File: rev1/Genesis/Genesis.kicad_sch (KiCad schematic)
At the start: 0 parts

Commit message: More updates.
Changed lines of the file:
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@@
 	(sheet
 		(at 100.33 90.17)
-		(size 19.05 21.59)
+		(size 19.05 24.13)
 		(exclude_from_sim no)
 		(in_bom yes)
@@
 		)
 		(property "Sheetfile" "../../kicad-import/adafruit-ethernet/Adafruit Ethernet FeatherWing.kicad_sch"
-			(at 100.33 112.3446 0)
+			(at 100.33 114.8846 0)
 			(effects
 				(font

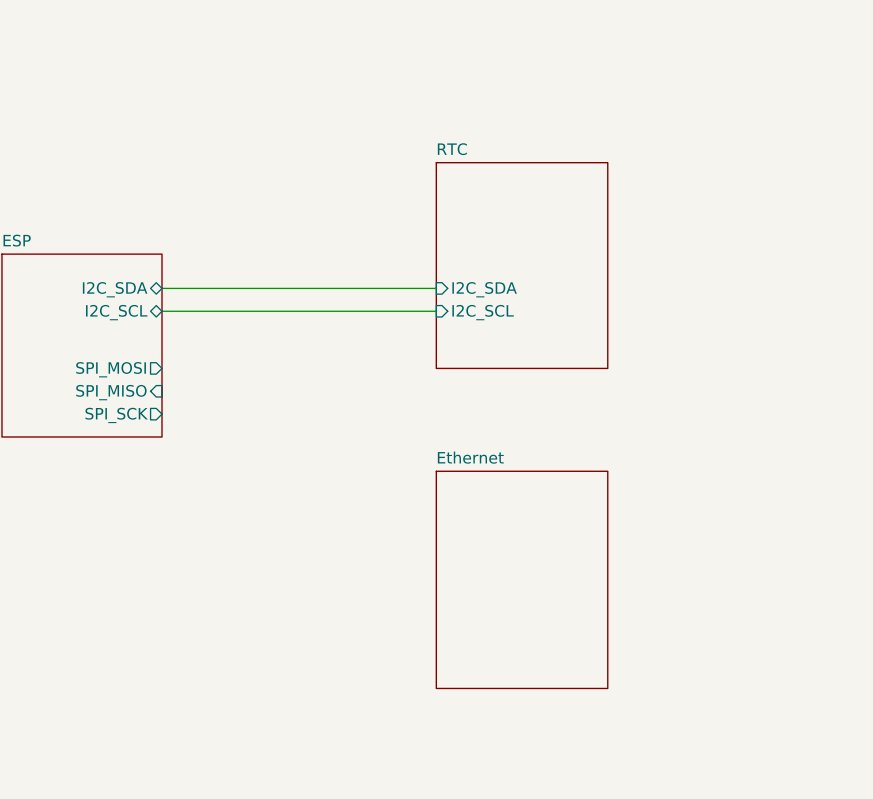
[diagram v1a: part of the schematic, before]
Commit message: Add and connect SPI sheet labels to Ethernet page.
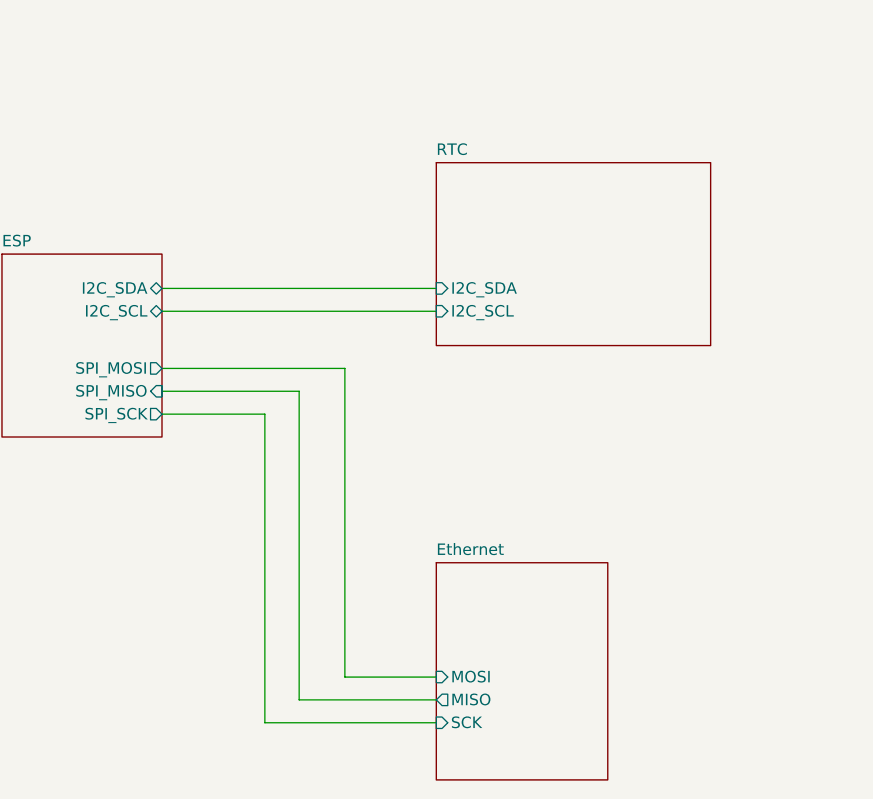
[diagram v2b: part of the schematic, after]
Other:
- sheet Ethernet ports: added MISO, MOSI, SCK; removed none
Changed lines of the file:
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@@
+	(wire
+		(pts
+			(xy 85.09 81.28) (xy 85.09 115.57)
+		)
+		(stroke
+			(width 0)
+			(type default)
+		)
+	)
+	(wire
+		(pts
+			(xy 85.09 115.57) (xy 100.33 115.57)
+		)
+		(stroke
+			(width 0)
+			(type default)
+		)
+	)
 	(wire
 		(pts
@@
 	(wire
 		(pts
+			(xy 69.85 78.74) (xy 90.17 78.74)
+		)
+		(stroke
+			(width 0)
+			(type default)
+		)
+	)
+	(wire
+		(pts
 			(xy 69.85 72.39) (xy 100.33 72.39)
+		)
+		(stroke
+			(width 0)
+			(type default)
+		)
+	)
+	(wire
+		(pts
+			(xy 81.28 118.11) (xy 100.33 118.11)
+		)
+		(stroke
+			(width 0)
+			(type default)
+		)
+	)
+	(wire
+		(pts
+			(xy 90.17 78.74) (xy 90.17 113.03)
+		)
+		(stroke
+			(width 0)
+			(type default)
+		)
+	)
+	(wire
+		(pts
+			(xy 69.85 81.28) (xy 85.09 81.28)
+		)
+		(stroke
+			(width 0)
+			(type default)
+		)
+	)
+	(wire
+		(pts
+			(xy 81.28 83.82) (xy 81.28 118.11)
+		)
+		(stroke
+			(width 0)
+			(type default)
+		)
+	)
+	(wire
+		(pts
+			(xy 90.17 113.03) (xy 100.33 113.03)
+		)
+		(stroke
+			(width 0)
+			(type default)
+		)
+	)
+	(wire
+		(pts
+			(xy 69.85 83.82) (xy 81.28 83.82)
 		)
 		(stroke
@@
 	)
 	(sheet
-		(at 100.33 90.17)
+		(at 100.33 100.33)
 		(size 19.05 24.13)
 		(exclude_from_sim no)
@@
 		)
 		(property "Sheetname" "Ethernet"
-			(at 100.33 89.4584 0)
+			(at 100.33 99.6184 0)
 			(effects
 				(font
@@
 		)
 		(property "Sheetfile" "../../kicad-import/adafruit-ethernet/Adafruit Ethernet FeatherWing.kicad_sch"
-			(at 100.33 114.8846 0)
+			(at 100.33 125.0446 0)
 			(effects
 				(font
@@
 				(justify left top)
 				(hide yes)
+			)
+		)
+		(pin "MISO" output
+			(at 100.33 115.57 180)
+			(effects
+				(font
+					(size 1.27 1.27)
+				)
+				(justify left)
+			)
+		)
+		(pin "MOSI" input
+			(at 100.33 113.03 180)
+			(effects
+				(font
+					(size 1.27 1.27)
+				)
+				(justify left)
+			)
+		)
+		(pin "SCK" input
+			(at 100.33 118.11 180)
+			(effects
+				(font
+					(size 1.27 1.27)
+				)
+				(justify left)
 			)
 		)
@@
 	(sheet
 		(at 100.33 55.88)
-		(size 19.05 22.86)
+		(size 30.48 20.32)
 		(exclude_from_sim no)
 		(in_bom yes)
@@
 		)
 		(property "Sheetfile" "../../kicad-import/adafruit-datalogger/adalogger featherwing.kicad_sch"
-			(at 100.33 79.3246 0)
-			(effects
-				(font
+			(at 100.33 76.7846 0)
+			(effects
+				(font

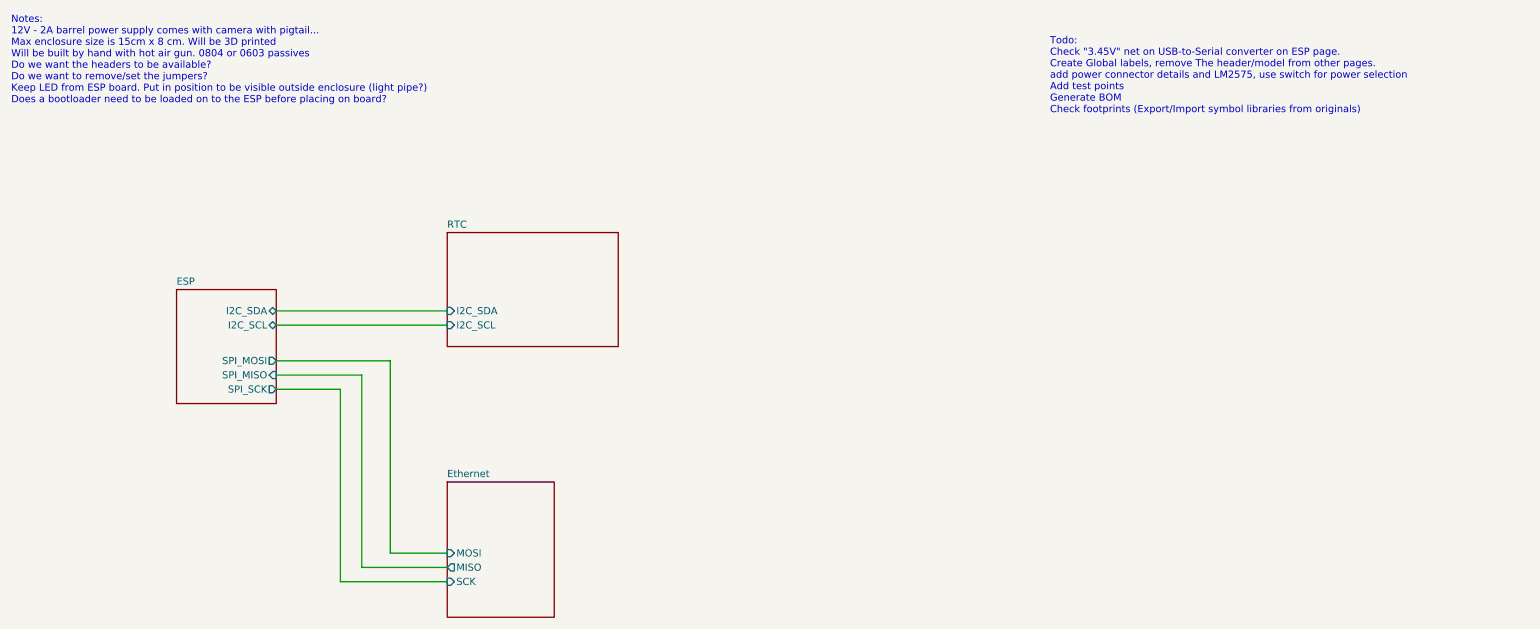
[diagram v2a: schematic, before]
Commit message: Improve sheet labels. Remove extra model and headers from ETH and RTC pages.
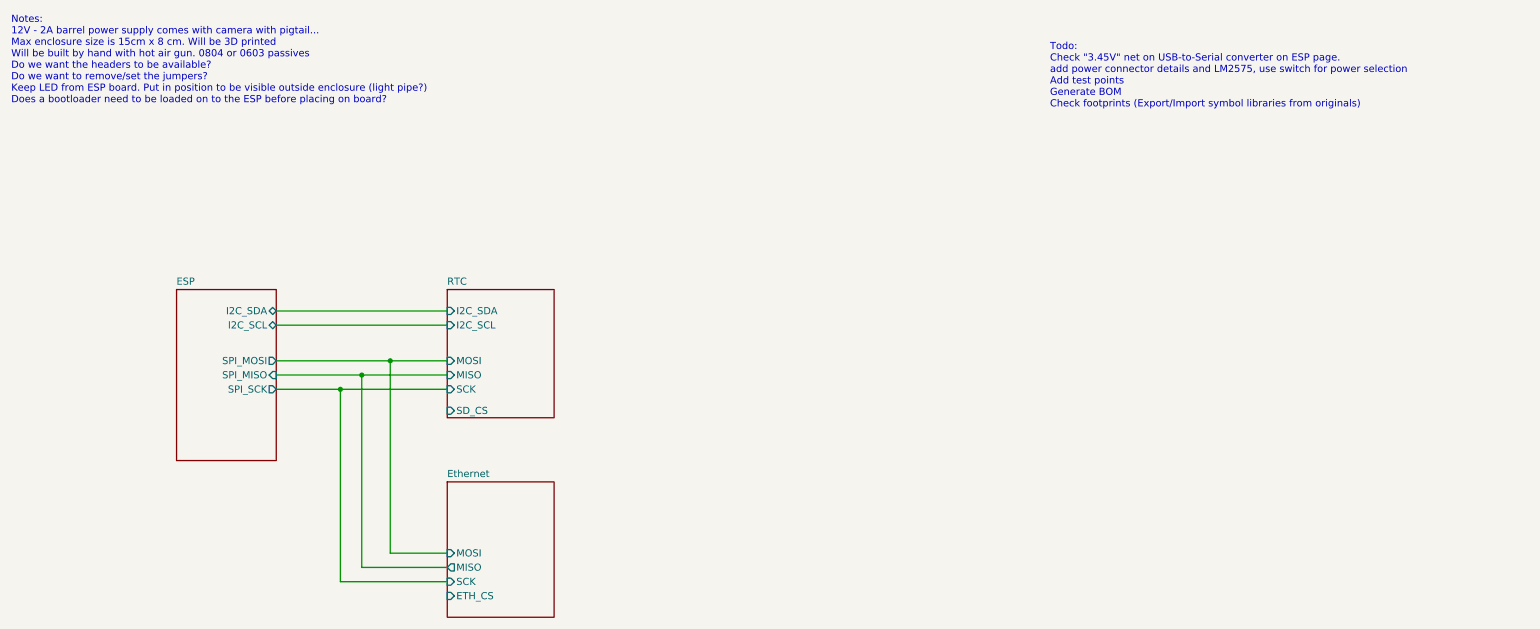
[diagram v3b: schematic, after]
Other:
- sheet Ethernet ports: added ETH_CS; removed none
- sheet RTC ports: added MISO, MOSI, SCK, SD_CS; removed none
- note added: "Todo: Check "3.45V" net on USB-to-Serial converter on ESP page. add power connector details and LM2575, use switch for power selection Add test points Generate BOM Check footprints (Export/Import symbol libraries from originals)"
- note removed: "Todo: Check "3.45V" net on USB-to-Serial converter on ESP page. Create Global labels, remove The header/model from other pages. add power connector details and LM2575, use switch for power selection Add test points Generate BOM Check footprints (Export/Import symbol libraries from originals)"
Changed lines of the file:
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@@
 		)
 	)
-	(text "Todo:\nCheck \"3.45V\" net on USB-to-Serial converter on ESP page.\nCreate Global labels, remove The header/model from other pages.\nadd power connector details and LM2575, use switch for power selection\nAdd test points\nGenerate BOM\nCheck footprints (Export/Import symbol libraries from originals)"
+	(text "Todo:\nCheck \"3.45V\" net on USB-to-Serial converter on ESP page.\nadd power connector details and LM2575, use switch for power selection\nAdd test points\nGenerate BOM\nCheck footprints (Export/Import symbol libraries from originals)"
 		(exclude_from_sim no)
 		(at 207.772 27.94 0)
@@
 		)
 	)
+	(junction
+		(at 85.09 81.28)
+		(diameter 0)
+		(color 0 0 0 0)
+	)
+	(junction
+		(at 81.28 83.82)
+		(diameter 0)
+		(color 0 0 0 0)
+	)
+	(junction
+		(at 90.17 78.74)
+		(diameter 0)
+		(color 0 0 0 0)
+	)
 	(wire
 		(pts
@@
 	(wire
 		(pts
+			(xy 81.28 83.82) (xy 100.33 83.82)
+		)
+		(stroke
+			(width 0)
+			(type default)
+		)
+	)
+	(wire
+		(pts
 			(xy 90.17 113.03) (xy 100.33 113.03)
 		)
@@
 		(pts
 			(xy 69.85 83.82) (xy 81.28 83.82)
+		)
+		(stroke
+			(width 0)
+			(type default)
+		)
+	)
+	(wire
+		(pts
+			(xy 85.09 81.28) (xy 100.33 81.28)
+		)
+		(stroke
+			(width 0)
+			(type default)
+		)
+	)
+	(wire
+		(pts
+			(xy 90.17 78.74) (xy 100.33 78.74)
 		)
 		(stroke
@@
 	(sheet
 		(at 52.07 66.04)
-		(size 17.78 20.32)
+		(size 17.78 30.48)
 		(exclude_from_sim no)
 		(in_bom yes)
@@
 		)
 		(property "Sheetfile" "../../kicad-import/adafruit-feather/Adafruit ESP32 Feather V2.kicad_sch"
-			(at 52.07 86.9446 0)
+			(at 52.07 97.1046 0)
 			(effects
 				(font
@@
 			)
 		)
+		(pin "ETH_CS" input
+			(at 100.33 120.65 180)
+			(effects
+				(font
+					(size 1.27 1.27)
+				)
+				(justify left)
+			)
+		)
 		(instances
 			(project "Genesis"
@@
 	)
 	(sheet
-		(at 100.33 55.88)
-		(size 30.48 20.32)
+		(at 100.33 66.04)
+		(size 19.05 22.86)
 		(exclude_from_sim no)
 		(in_bom yes)
@@
 		)
 		(property "Sheetname" "RTC"
-			(at 100.33 55.1684 0)
+			(at 100.33 65.3284 0)
 			(effects
 				(font
@@
 		)
 		(property "Sheetfile" "../../kicad-import/adafruit-datalogger/adalogger featherwing.kicad_sch"
-			(at 100.33 76.7846 0)
+			(at 100.33 89.4846 0)
 			(effects
 				(font
@@
 			(effects
 				(font
+					(size 1.27 1.27)
+				)
+				(justify left)
+			)
+		)
+		(pin "MISO" input
+			(at 100.33 81.28 180)
+			(effects
+				(font
+					(size 1.27 1.27)
+				)
+				(justify left)
+			)
+		)
+		(pin "MOSI" input
+			(at 100.33 78.74 180)
+			(effects
+				(font
+					(size 1.27 1.27)
+				)
+				(justify left)
+			)
+		)
+		(pin "SCK" input
+			(at 100.33 83.82 180)
+			(effects
+				(font
+					(size 1.27 1.27)
+				)
+				(justify left)
+			)
+		)
+		(pin "SD_CS" input
+			(at 100.33 87.63 180)
+			(effects
+				(font

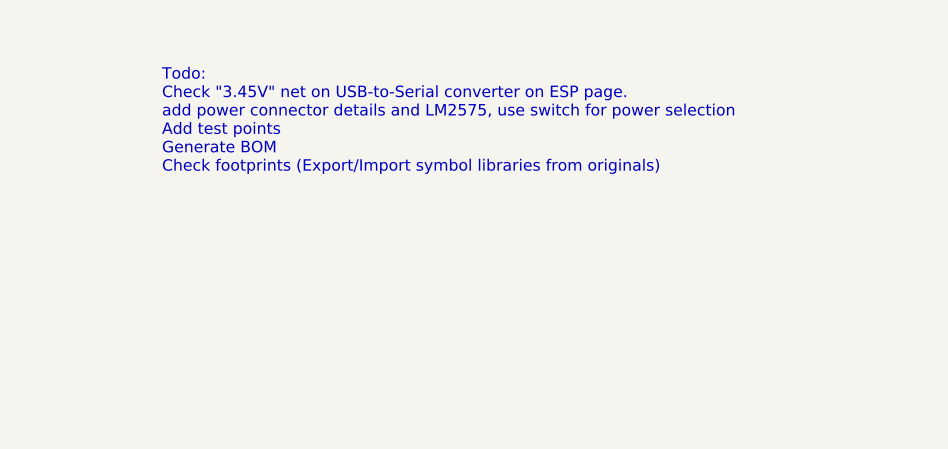
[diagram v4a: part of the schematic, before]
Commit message: Do rough major component placement for layout
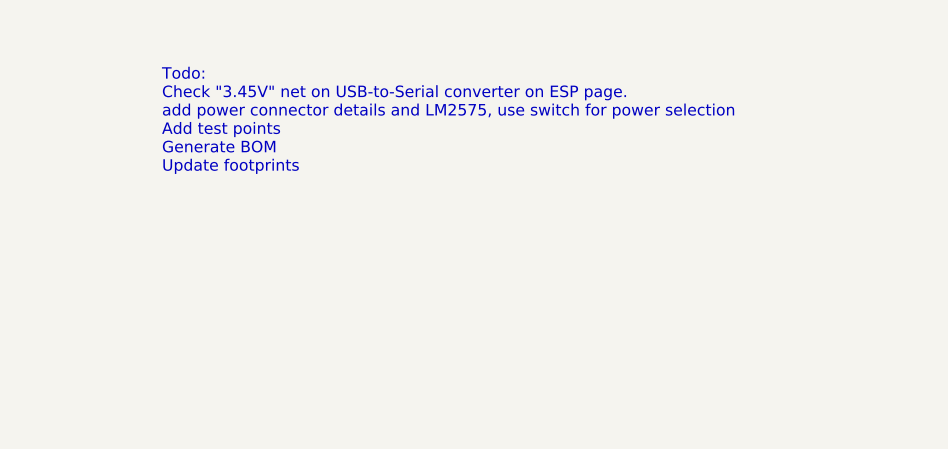
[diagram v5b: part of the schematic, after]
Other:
- note added: "Todo: Check "3.45V" net on USB-to-Serial converter on ESP page. add power connector details and LM2575, use switch for power selection Add test points Generate BOM Update footprints"
- note removed: "Todo: Check "3.45V" net on USB-to-Serial converter on ESP page. add power connector details and LM2575, use switch for power selection Add test points Generate BOM Check footprints (Export/Import symbol libraries from originals)"
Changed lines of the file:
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@@
 		)
 	)
-	(text "Todo:\nCheck \"3.45V\" net on USB-to-Serial converter on ESP page.\nadd power connector details and LM2575, use switch for power selection\nAdd test points\nGenerate BOM\nCheck footprints (Export/Import symbol libraries from originals)"
+	(text "Todo:\nCheck \"3.45V\" net on USB-to-Serial converter on ESP page.\nadd power connector details and LM2575, use switch for power selection\nAdd test points\nGenerate BOM\nUpdate footprints"
 		(exclude_from_sim no)
 		(at 207.772 27.94 0)
